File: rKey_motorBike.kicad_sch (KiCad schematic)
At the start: 5 parts

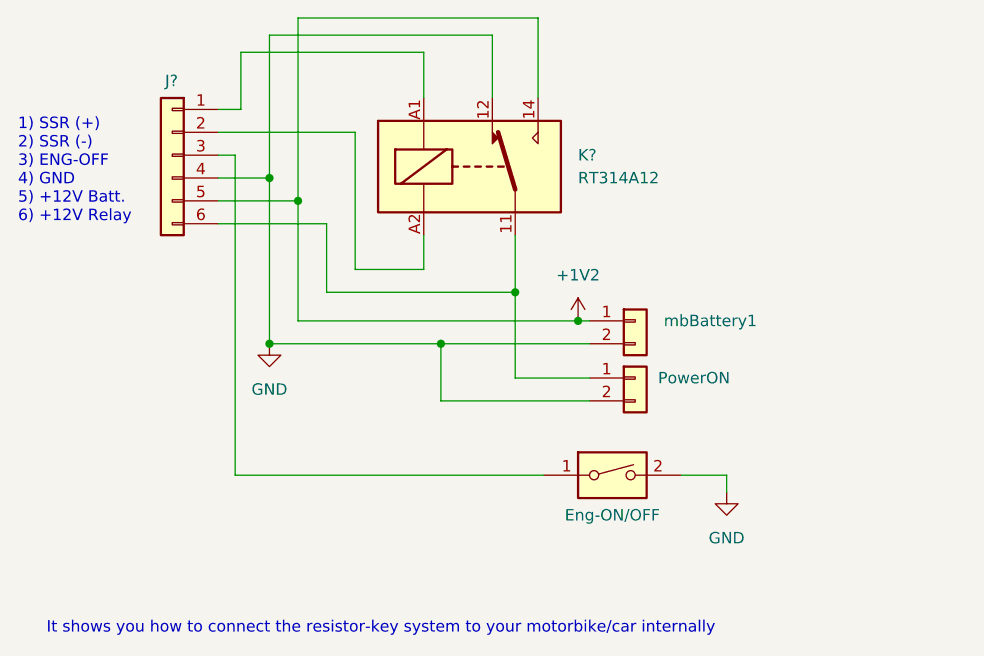
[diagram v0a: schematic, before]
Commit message: fix: updates to the new rKey schema
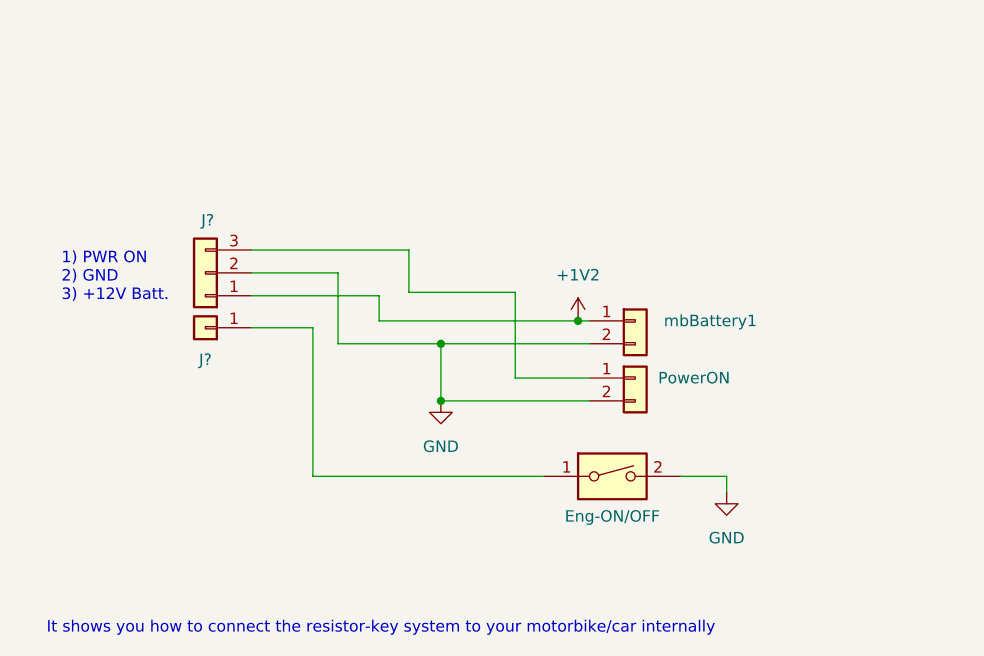
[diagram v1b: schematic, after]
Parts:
- removed J?: Conn_01x06, Connector_PinHeader_2.54mm:PinHeader_1x06_P2.54mm_Vertical, symbol Connector_Generic:Conn_01x06
- removed K?: RT314A12, Relay_THT:Relay_SPDT_Schrack-RT1-16A-FormC_RM5mm, symbol Relay:RT314A12
- added J?: Conn_01x01, symbol Connector_Generic:Conn_01x01
- added J?: Conn_01x03, symbol Connector_Generic:Conn_01x03
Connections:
- net +1V2: now also J?.1 (Pin_1)
- net GND: now also J?.2 (Pin_2)
- net at Eng-ON/OFF.1: now also J?.1 (Pin_1)
- net at PowerON.1 (Pin_1): now also J?.3 (Pin_3)
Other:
- note added: "1) PWR ON 2) GND 3) +12V Batt."
- note removed: "1) SSR (+) 2) SSR (-) 3) ENG-OFF 4) GND 5) +12V Batt. 6) +12V Relay"
